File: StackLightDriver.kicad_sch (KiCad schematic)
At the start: 69 parts, among them J1 B2B-XH-A, J10 B2B-XH-A, J11 PJ-102AH, J12 USB_C_Receptacle_USB2.0_14P, J2 B2B-XH-A, J3 B2B-XH-A, J4 B2B-XH-A, J5 B2B-XH-A, J6 B2B-XH-A, J7 B2B-XH-A, J8 B2B-XH-A, J9 B2B-XH-A, P1 282837-2, P2 282837-2, P3 282837-2, P4 282837-2, U6 ESP32-S3-WROOM-1-N4, U8 USBLC6-2SC6

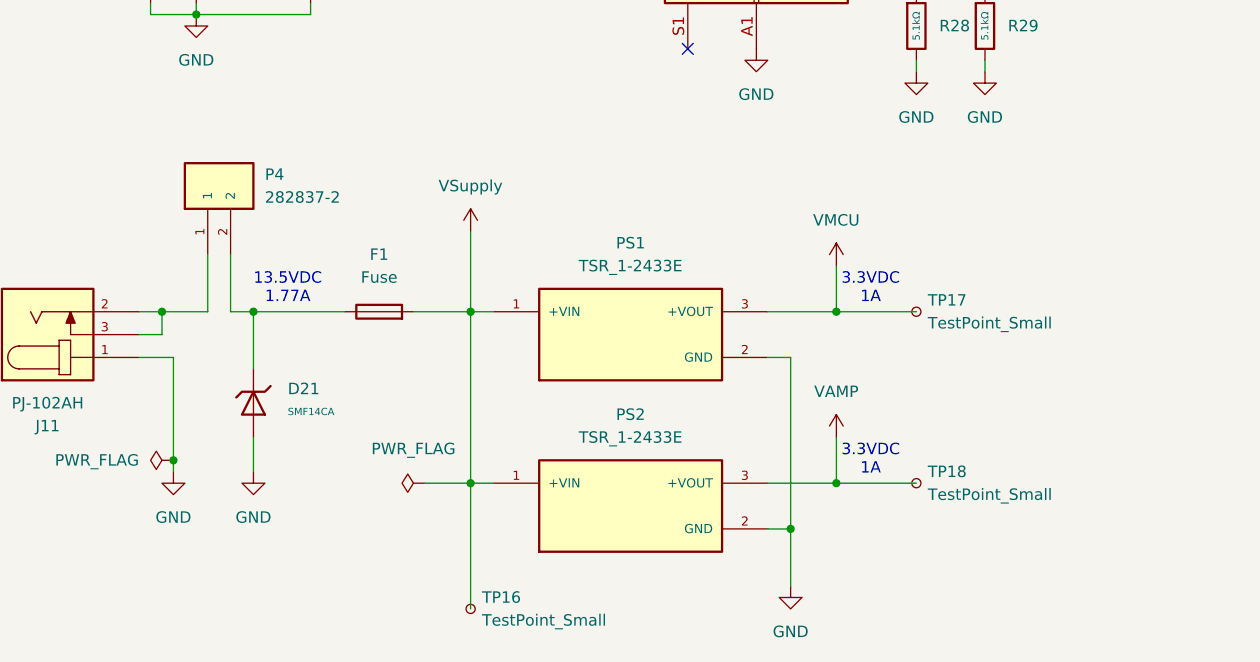
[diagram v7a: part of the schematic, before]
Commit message: Removed Test Points, reordered fuse and switch
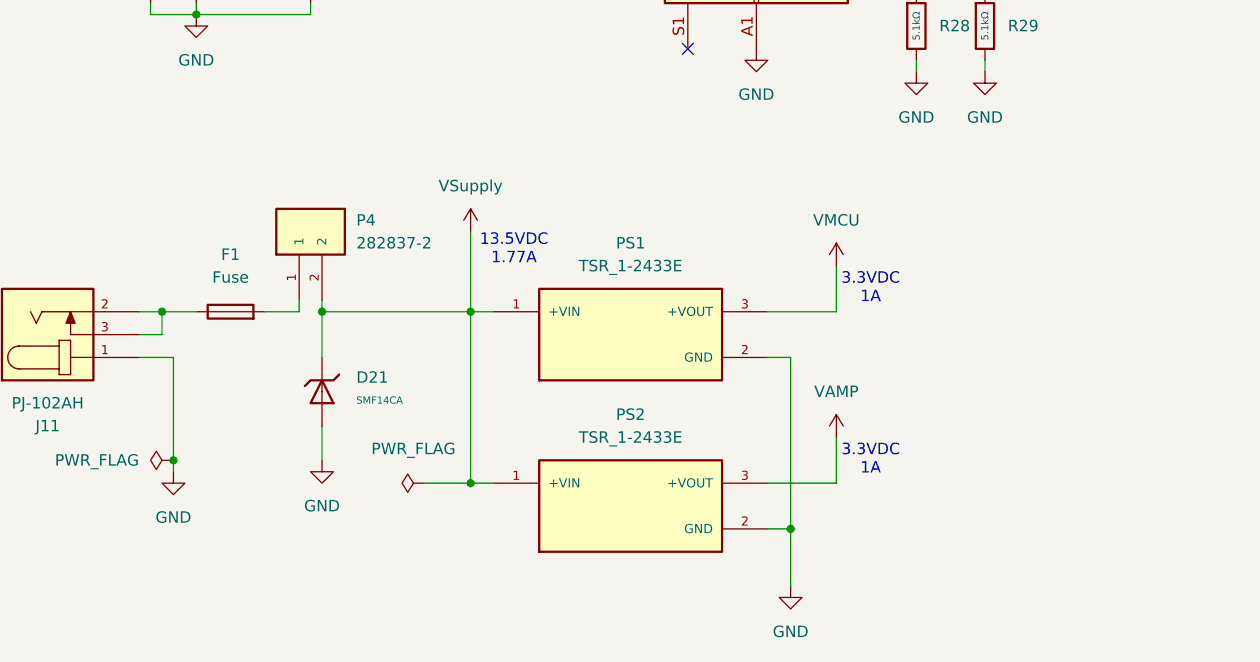
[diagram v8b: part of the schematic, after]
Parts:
- removed TP16, TP17, TP18: TestPoint_Small, symbol Connector:TestPoint_Small
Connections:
- net VSupply: now also D21.1, P4.2; no longer F1.2
- net at J11.2, J11.3: now also F1.1; no longer P4.1
- new net: F1.2, P4.1
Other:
- moved on the sheet: D21, F1, P4
